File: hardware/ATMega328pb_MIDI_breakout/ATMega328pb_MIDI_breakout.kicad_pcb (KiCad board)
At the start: 2 copper layers, 68.7 x 101.3 mm, 38 parts, among them J1 USB_B, J2 MIDI OUT, J3 MIDI IN, J4 I2C, J5 Conn_01x15_Male, J6 Conn_01x15_Male, J7 Barrel_Jack_Switch, Q1 2N3906, SW1 RotaryEncoder_Switch, SW2 SW_Push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

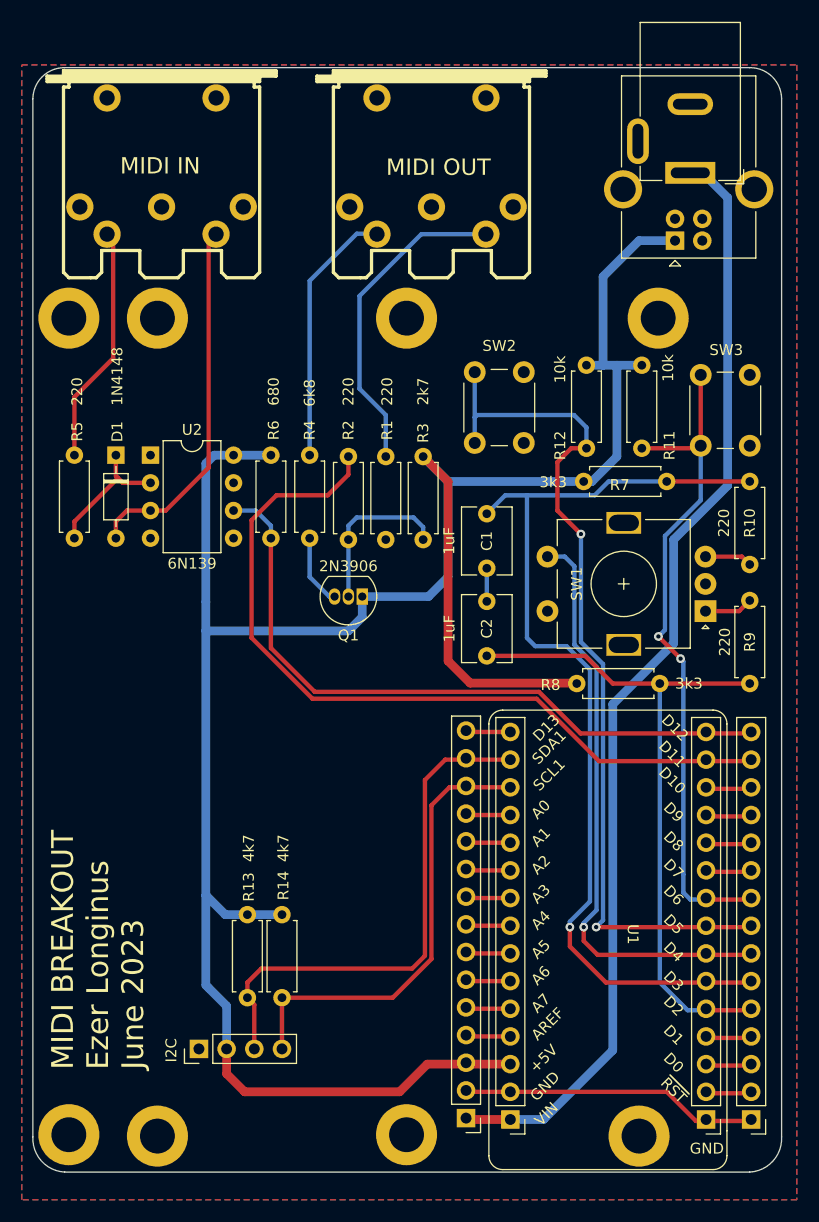
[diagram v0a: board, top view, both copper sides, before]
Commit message: MIDI Breakout Variations
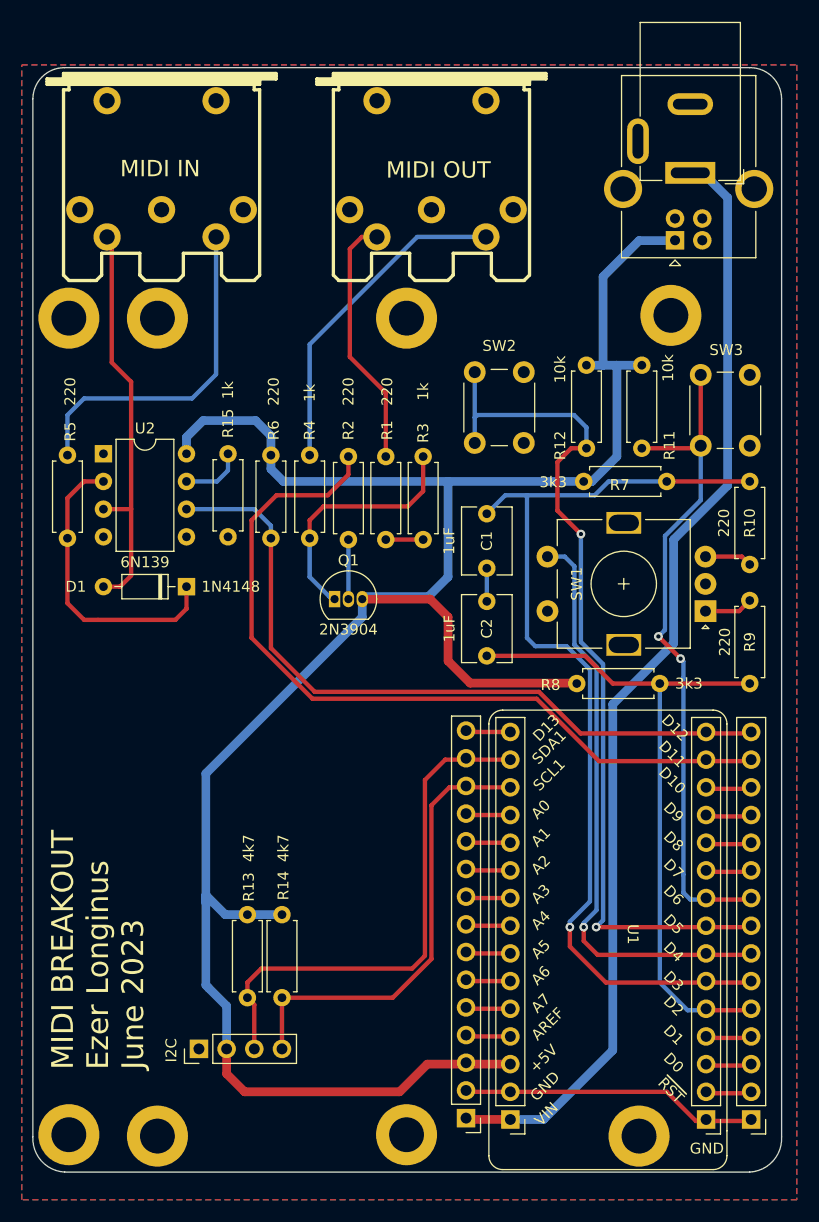
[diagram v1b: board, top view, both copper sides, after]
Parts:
- added R15: 1k, Resistor_THT:R_Axial_DIN0207_L6.3mm_D2.5mm_P7.62mm_Horizontal, F.Cu at (131.3, 90.9)
- Q1: value 2N3906 -> 2N3904
- R2: value 6k8 -> 1k
- R3: value 2k7 -> 1k
- R6: value 680 -> 220
- moved D1 13.7 mm to (127.5, 103.1), turned to 180 degrees
- moved H4 5.72 mm to (172.0, 78.2)
- moved U2 4.32 mm to (119.9, 90.9)
- moved Q1 2.55 mm to (141.1, 104.3), turned to 0 degrees
- moved R5 0.64 mm to (116.6, 91.1)
- moved J2 0.25 mm to (150.0, 65.5)
- moved J3 0.25 mm to (125.2, 65.5)
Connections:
- J3 pad 4: Net-(J3-Pad4) -> Net-(D1-Pad2)
- J3 pad 5: Net-(D1-Pad2) -> Net-(J3-Pad5)
- Q1 pad 1: +5V -> Net-(Q1-Pad1)
- Q1 pad 3: Net-(Q1-Pad3) -> +5V
- R1 pad 1: Net-(J2-Pad5) -> Net-(J2-Pad4)
- R3 pad 1: +5V -> Net-(Q1-Pad1)
- R3 pad 2: Net-(Q1-Pad2) -> GND
- R4 pad 1: Net-(Q1-Pad3) -> Net-(Q1-Pad1)
- R4 pad 2: Net-(J2-Pad4) -> Net-(J2-Pad5)
- R5 pad 1: Net-(J3-Pad4) -> Net-(J3-Pad5)
- U2 pad 7: unconnected-(U2-Pad7) -> Net-(U2-Pad7)
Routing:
- net Net-(J3-Pad5): track 0.00 -> 32.0 mm
- net Net-(Q1-Pad1): track 0.00 -> 22.9 mm
- net Net-(J3-Pad4): track 22.0 -> 0.00 mm
- net Net-(D1-Pad1): track 12.5 -> 27.6 mm
- net Net-(Q1-Pad2): track 15.2 -> 5.23 mm
- net +5V: track 214.3 -> 205.6 mm
- net Net-(Q1-Pad3): track 6.59 -> 0.00 mm
- net Net-(U2-Pad7): track 0.00 -> 5.75 mm
- net Net-(D1-Pad2): track 34.1 -> 38.5 mm
- net RX1: track 62.4 -> 66.8 mm
- net GND: track 30.2 -> 33.6 mm
- net Net-(J2-Pad5): track 29.7 -> 30.4 mm
- net Net-(J2-Pad4): track 24.0 -> 23.4 mm

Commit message: Fixed MIDI pinout swap
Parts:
- added D2: LED, LED_THT:LED_D5.0mm, F.Cu at (163.3, 78.5)
- added D3: LED, LED_THT:LED_D5.0mm, F.Cu at (154.7, 78.5)
- added J8: I2C, Connector_PinHeader_2.54mm:PinHeader_1x04_P2.54mm_Vertical, F.Cu at (121.5, 147.9)
- added J9: Conn_01x15_Male, Connector_PinHeader_2.54mm:PinHeader_1x15_P2.54mm_Vertical, F.Cu at (160.0, 152.0)
- added R16: 1k, Resistor_THT:R_Axial_DIN0207_L6.3mm_D2.5mm_P7.62mm_Horizontal, F.Cu at (168.4, 90.4)
- added R17: 1k, Resistor_THT:R_Axial_DIN0207_L6.3mm_D2.5mm_P7.62mm_Horizontal, F.Cu at (165.1, 90.4)
- moved J4 9.27 mm to (128.9, 136.3)
- moved R13 9.27 mm to (133.3, 131.6)
- moved R14 9.27 mm to (136.5, 131.6)
- moved R11 2.41 mm to (171.7, 90.4)
- moved R12 2.41 mm to (161.8, 90.4)
- moved SW3 0.48 mm to (175.0, 89.9)
- moved SW2 0.07 mm to (154.0, 89.9)
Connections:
- net Net-(J5-Pad10) renamed D7
- net Net-(J5-Pad11) renamed D8
- J3 pad 4: Net-(D1-Pad2) -> Net-(J3-Pad4)
- J3 pad 5: Net-(J3-Pad5) -> Net-(D1-Pad2)
- R5 pad 1: Net-(J3-Pad5) -> Net-(J3-Pad4)
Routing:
- net D7: track 4.02 -> 50.9 mm, vias 0 -> 1
- net D8: track 4.02 -> 46.2 mm, vias 0 -> 1
- net Net-(J3-Pad5): track 32.0 -> 0.00 mm
- net Net-(J3-Pad4): track 0.00 -> 22.1 mm
- net SCL1: track 41.9 -> 56.0 mm
- net +5V: track 205.6 -> 219.3 mm
- net SDA1: track 48.4 -> 60.7 mm
- net Net-(D3-Pad2): track 0.00 -> 10.6 mm
- net Net-(D2-Pad2): track 0.00 -> 6.11 mm
- net +VDC: track 103.1 -> 106.3 mm
- net Net-(J6-Pad9): track 4.06 -> 6.86 mm
- net Net-(J6-Pad8): track 4.06 -> 6.86 mm
- net Net-(J6-Pad7): track 4.06 -> 6.86 mm
- net Net-(J6-Pad6): track 4.06 -> 6.86 mm
- net Net-(J6-Pad5): track 4.06 -> 6.86 mm
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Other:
- board text added: "MIDI BREAKOUT Ezer Longinus July 2023"
- board text added: "SCL"
- board text added: "SDA"
- board text removed: "MIDI BREAKOUT Ezer Longinus June 2023"
